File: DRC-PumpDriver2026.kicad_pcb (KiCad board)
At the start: 2 copper layers, 60 x 45 mm, 63 parts, among them J1 STLINK, J10 VIN_PWR, J2 CAN, J3 CAN, J4 PUMP1, J5 PUMP2, J6 PUMP3, J7 PUMP4, J8 PUMP5, J9 PUMP6, SW1 SW_Push, SW2 DIP, SW3 SS-12D00G3, U2 STM32F303K8Tx, U3 TLP241A, U4 TLP241A, U5 TLP241A, U6 TLP241A, U7 TLP241A, U8 TLP241A, U9 RT9080-33GJ5

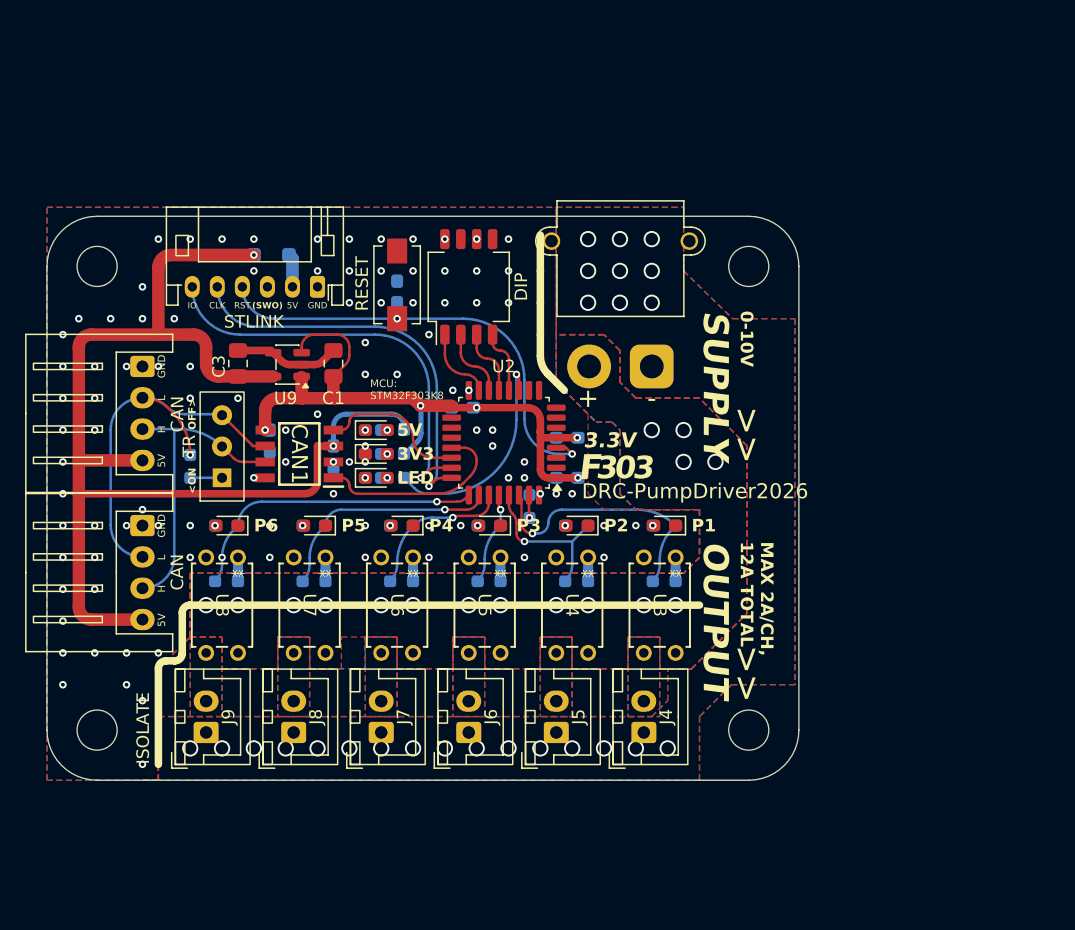
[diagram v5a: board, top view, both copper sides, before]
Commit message: STLINK書込みをボックスヘッダへ、USB追加、v0.1.0
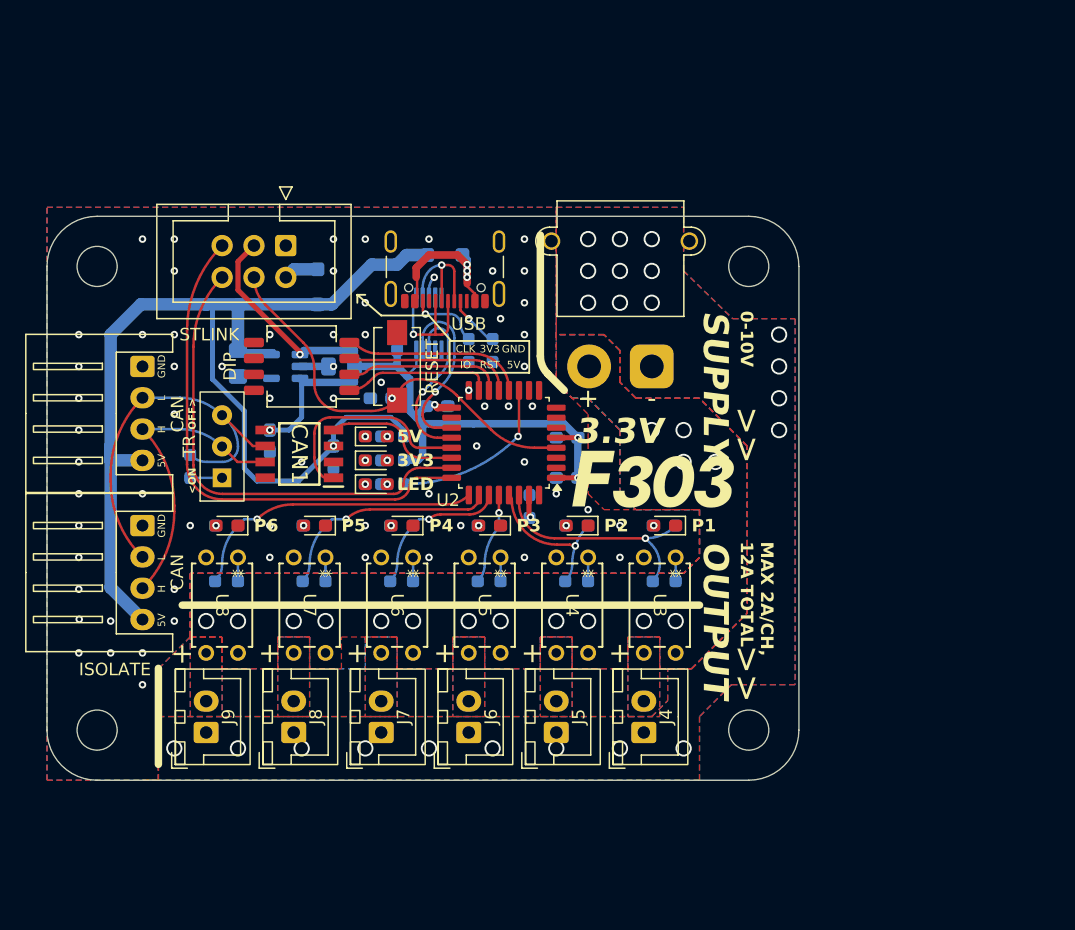
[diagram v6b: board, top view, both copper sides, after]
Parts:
- added C9: 0.1u, Capacitor_SMD:C_0603_1608Metric_Pad1.08x0.95mm_HandSolder, B.Cu at (141.0, 84.8)
- added D11: SS2040FL, Diode_SMD:D_SOD-123F, B.Cu at (144.8, 78.1)
- added R18: 5.1k, Resistor_SMD:R_0603_1608Metric_Pad0.98x0.95mm_HandSolder, B.Cu at (148.6, 85.7)
- added R19: 5.1k, Resistor_SMD:R_0603_1608Metric_Pad0.98x0.95mm_HandSolder, B.Cu at (146.7, 85.7)
- added U9: CH340E, Package_SO:MSOP-10_3x3mm_P0.5mm, B.Cu at (143.5, 83.6)
- added USB: USB_C, Connector_USB:USB_C_Receptacle_GCT_USB4105-xx-A_16P_TopMnt_Horizontal, F.Cu at (144.8, 78.1)
- C1, C3: moved to B.Cu
- R2, R4: value 470 -> 1k
- STLINK: renamed from J1; footprint Connector_JST:JST_PH_S6B-PH-K_1x06_P2.00mm_Horizontal -> Connector_IDC:IDC-Header_2x03_P2.54mm_Vertical
- U1: renamed from U9; moved to B.Cu
- moved REF** 37.1 mm to (168.3, 104.9), turned to -90 degrees
- moved SW2 14.8 mm to (133.3, 87.0), turned to 180 degrees
- moved C2 8.58 mm to (139.7, 89.5), turned to 180 degrees
- moved SW1 6.51 mm to (141.0, 87.0)
- moved D1 4.47 mm to (134.6, 80.6), turned to 90 degrees
- moved STLINK 4.16 mm to (132.1, 77.3), turned to -90 degrees
- moved C5 2.04 mm to (144.1, 90.2), turned to 0 degrees
- moved C1 0.68 mm to (136.5, 87.0), turned to 180 degrees
- moved D2 0.51 mm to (139.3, 94.5)
- moved D3 0.51 mm to (139.3, 92.6)
- moved D4 0.51 mm to (139.3, 96.4)
- moved R2 0.51 mm to (140.6, 94.5)
- moved R3 0.51 mm to (140.6, 92.6)
- moved R4 0.51 mm to (140.6, 96.4)
- moved G*** 0.36 mm to (168.0, 87.0), turned to -90 degrees
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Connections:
- STLINK pad 3: /SWO -> +3V3
- U2 pad 19: unconnected-(U2-PA9-Pad19) -> /USART1_TX
- U2 pad 20: unconnected-(U2-PA10-Pad20) -> /USART1_RX
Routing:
- net +3V3: track 51.2 -> 70.7 mm
- net /USART1_TX: track 0.00 -> 14.3 mm, vias 0 -> 1
- net Net-(D11-A): track 0.00 -> 14.2 mm, vias 0 -> 3
- net /USART1_RX: track 0.00 -> 13.8 mm, vias 0 -> 1
- net /USB_UART/USB_D_P: track 0.00 -> 10.9 mm, vias 0 -> 1
- net /USB_UART/USB_D_N: track 0.00 -> 9.91 mm, vias 0 -> 1
- net /SWCLK: track 31.9 -> 41.7 mm, vias 1 -> 0
- net /DIP4: track 5.15 -> 14.6 mm
- net /DIP3: track 5.40 -> 13.5 mm
- net /DIP2: track 5.65 -> 12.6 mm
- net /DIP1: track 5.90 -> 11.9 mm
- net Net-(J11-CC2): track 0.00 -> 5.73 mm, vias 0 -> 1
- net /SWDIO: track 33.3 -> 38.5 mm, vias 1 -> 0
- net GND: track 8.46 -> 4.01 mm, vias 104 -> 69
- net Net-(J11-CC1): track 0.00 -> 4.25 mm, vias 0 -> 1
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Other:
- board text added: "+"
- board text added: "3V3"
- board text added: "v0.1.0"
- board text removed: "(SWO)"
- board text removed: "0"
- board text removed: "3"
- board text removed: "6ch Pump Driver"
- board text removed: "DRC-PumpDriver2026 v0.0.2"
- board text removed: "F"
- board text removed: "MCU: STM32F303K8"

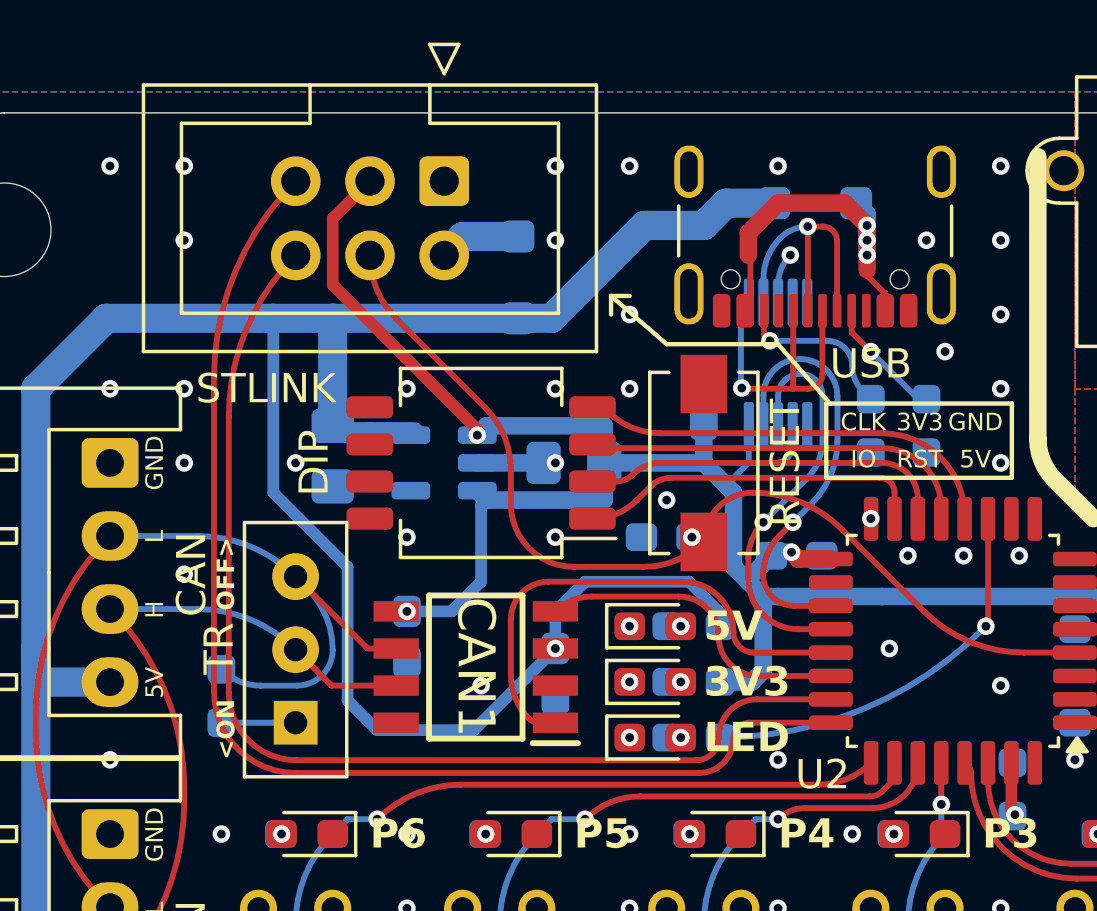
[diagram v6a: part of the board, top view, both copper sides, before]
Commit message: レギュレータのフットプリントを修正
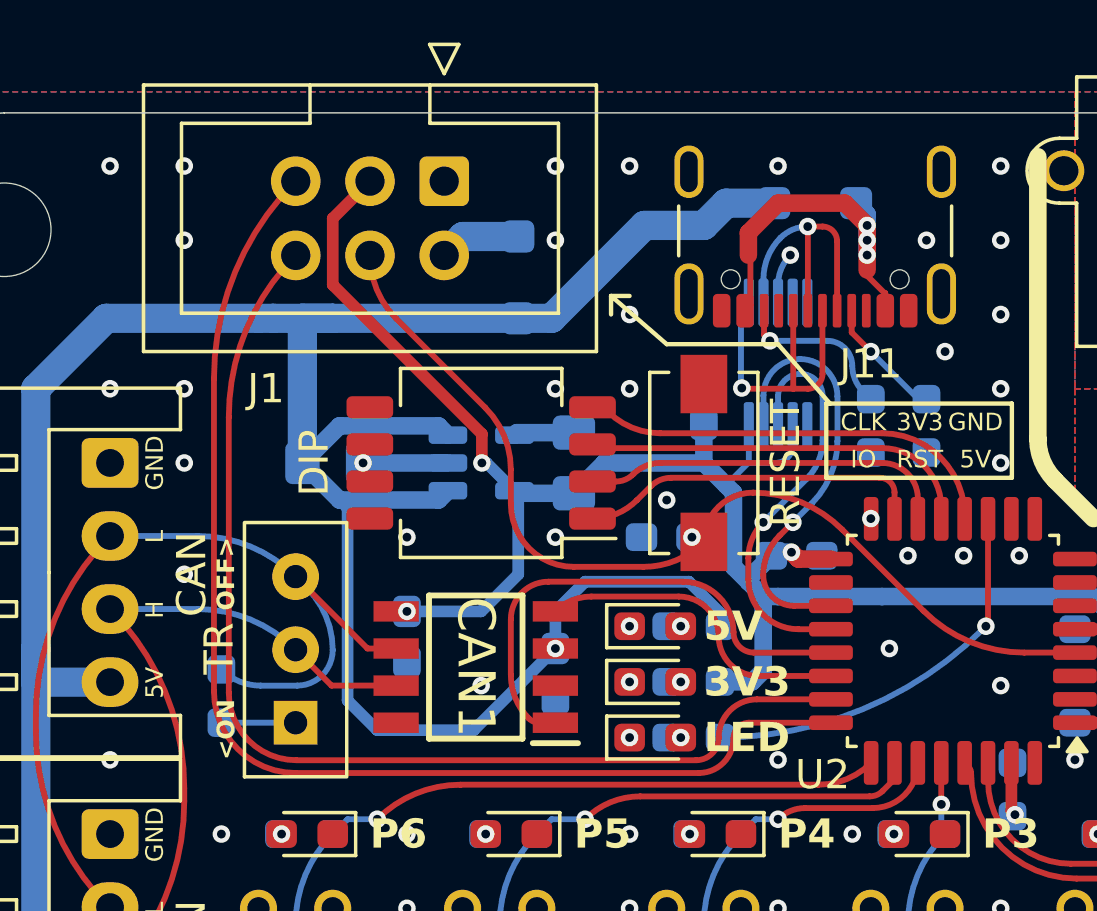
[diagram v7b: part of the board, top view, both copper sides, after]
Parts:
- R11, R13, R15, R5, R7, R9: value 470 -> 1k
- moved C3 8.26 mm to (136.5, 87.0), turned to 90 degrees
- moved C1 8.25 mm to (128.3, 87.0), turned to 0 degrees
- moved U1 1.27 mm to (133.3, 87.0), turned to 0 degrees
- renumbered STLINK to J1, USB to J11
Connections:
- C1 pad 1: +3V3 -> +5V
- C3 pad 1: +5V -> +3V3
- U1 pad 1: +3V3 -> +5V
- U1 pad 3: +3V3 -> +5V
- U1 pad 5: +5V -> +3V3
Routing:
- net +3V3: track 70.7 -> 66.8 mm
- net +5V: track 93.0 -> 96.5 mm
- net GND: track 4.01 -> 6.71 mm, vias 69 -> 67
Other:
- board text added: "${REFERENCE}"
- board text added: "v0.1.1"
- board text removed: "v0.1.0"
